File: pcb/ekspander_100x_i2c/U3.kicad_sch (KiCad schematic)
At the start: 6 parts, among them J10 DG127A-5.08-06P-14-00AH, J11 DG127A-5.08-06P-14-00AH, J8 DG127A-5.08-06P-14-00AH, J9 DG127A-5.08-06P-14-00AH, U3 MCP23017_SP, U4 MCP23017_SP

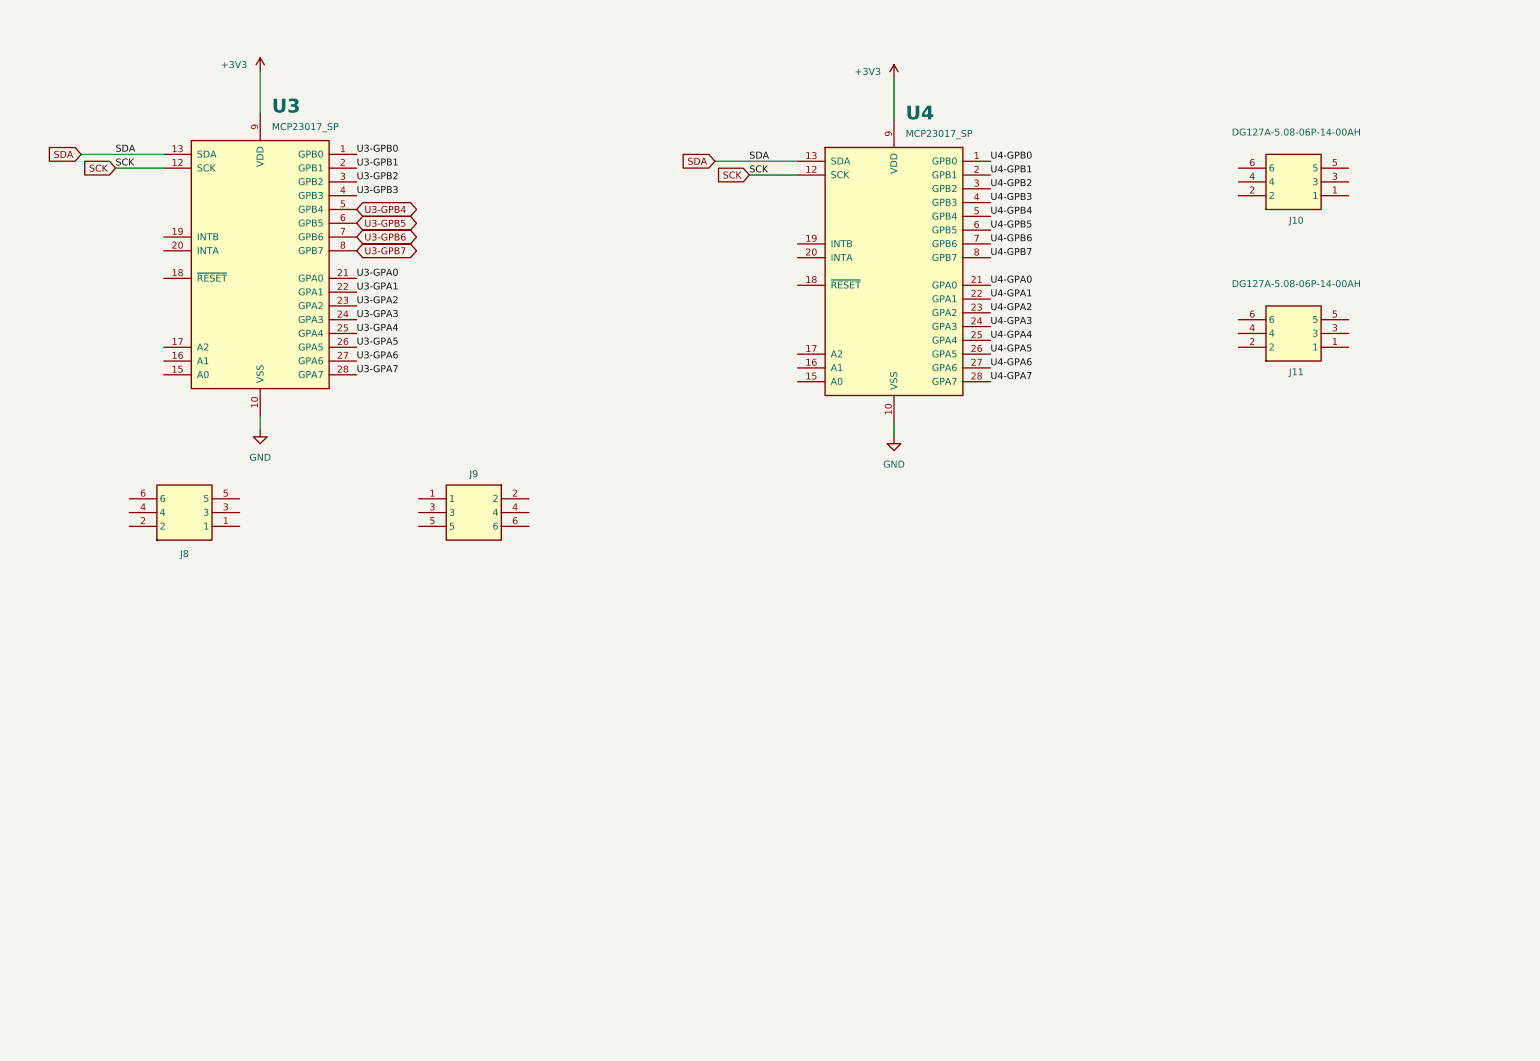
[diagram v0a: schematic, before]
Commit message: Ekspander U2 - U3 - U4 update
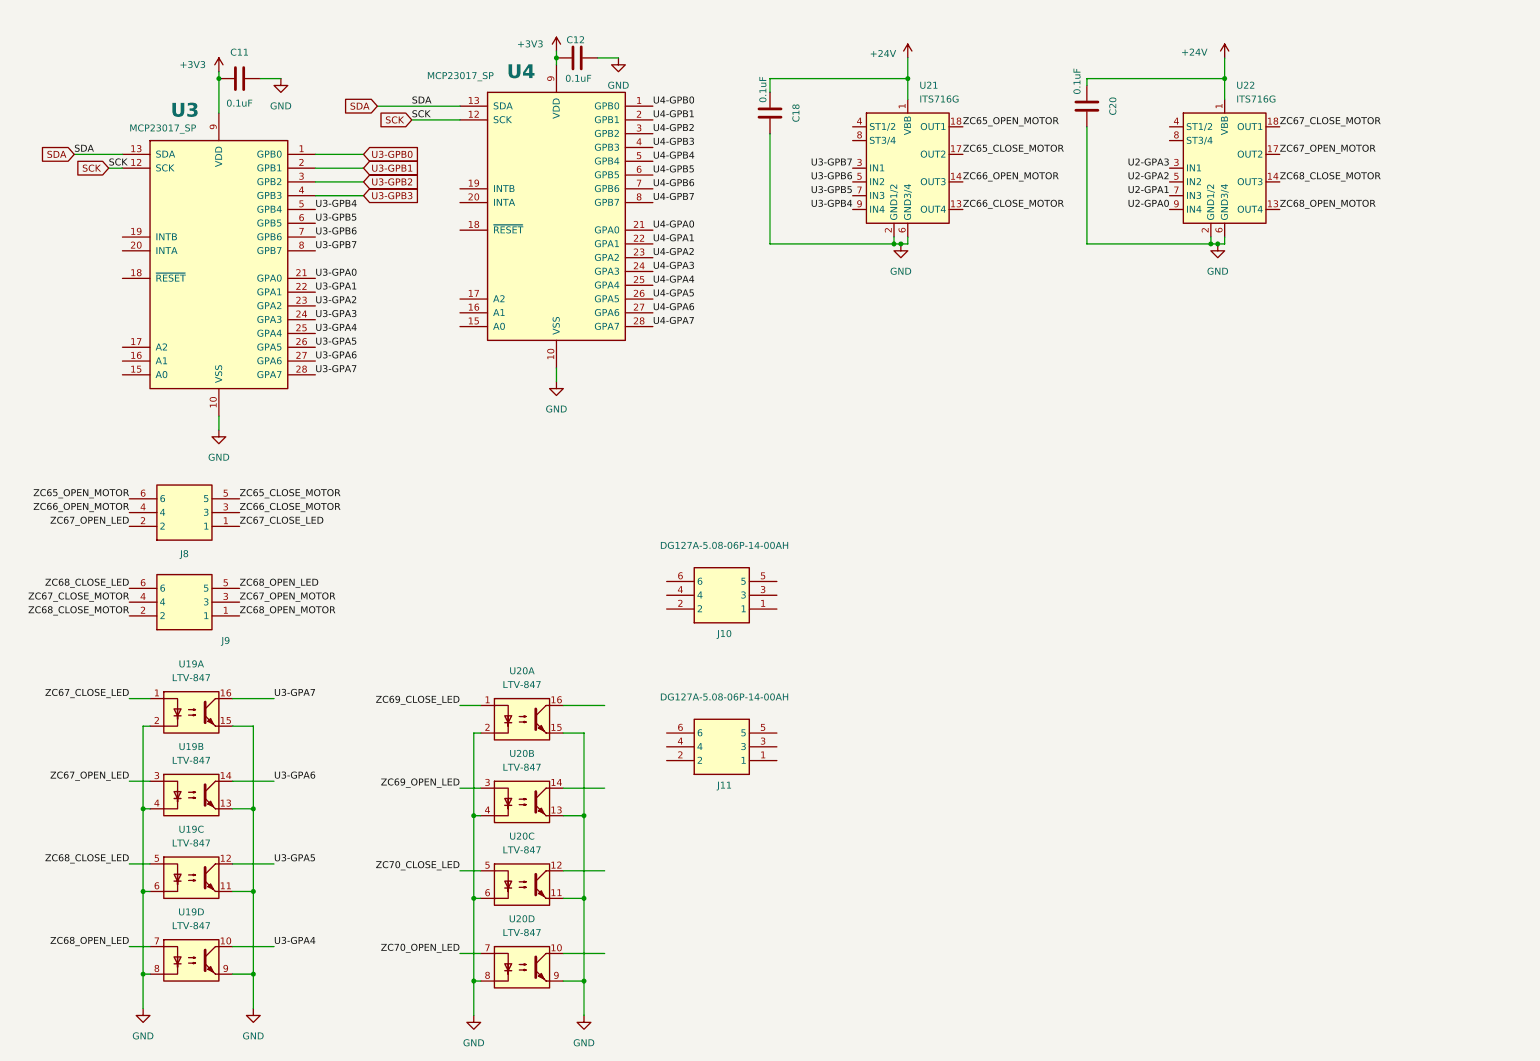
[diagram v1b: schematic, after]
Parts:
- added C11, C12, C18, C20: 0.1uF, Capacitor_SMD:C_0805_2012Metric_Pad1.18x1.45mm_HandSolder, symbol Device:C
- added U19, U20: LTV-847, Package_DIP:DIP-16_W7.62mm, symbol Isolator:LTV-847
- added U21, U22: ITS716G, Package_SO:SOIC-20W_7.5x12.8mm_P1.27mm, symbol Driver_FET:ITS716G
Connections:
- net +3V3: now also C11.1, C12.1
- net GND: now also C11.2, C12.2, C18.2, C20.2, U19.11, U19.13, U19.15, U19.2, U19.4, U19.6, U19.8, U19.9, U20.11, U20.13, U20.15, U20.2, U20.4, U20.6, U20.8, U20.9, U21.2 (GND1/2), U21.6 (GND3/4), U22.2 (GND1/2), U22.6 (GND3/4)
- net U3-GPA4: now also U19.10
- net U3-GPA5: now also U19.12
- net U3-GPA6: now also U19.14
- net U3-GPA7: now also U19.16
- net U3-GPB4: now also U21.9 (IN4)
- net U3-GPB5: now also U21.7 (IN3)
- net U3-GPB6: now also U21.5 (IN2)
- net U3-GPB7: now also U21.3 (IN1)
- net ZC67_CLOSE_LED: now reaches J8.1
- net ZC67_CLOSE_LED: now also U19.1
- net ZC67_OPEN_LED: now reaches J8.2
- net ZC67_OPEN_LED: now also U19.3
- net ZC66_CLOSE_MOTOR: now reaches J8.3
- net ZC66_CLOSE_MOTOR: now also U21.13 (OUT4)
- net ZC66_OPEN_MOTOR: now reaches J8.4
- net ZC66_OPEN_MOTOR: now also U21.14 (OUT3)
- net ZC65_CLOSE_MOTOR: now reaches J8.5
- net ZC65_CLOSE_MOTOR: now also U21.17 (OUT2)
- net ZC65_OPEN_MOTOR: now reaches J8.6
- net ZC65_OPEN_MOTOR: now also U21.18 (OUT1)
- net ZC68_OPEN_MOTOR: now reaches J9.1
- net ZC68_OPEN_MOTOR: now also U22.13 (OUT4)
- net ZC68_CLOSE_MOTOR: now reaches J9.2
- net ZC68_CLOSE_MOTOR: now also U22.14 (OUT3)
- net ZC67_OPEN_MOTOR: now reaches J9.3
- net ZC67_OPEN_MOTOR: now also U22.17 (OUT2)
- net ZC67_CLOSE_MOTOR: now reaches J9.4
- net ZC67_CLOSE_MOTOR: now also U22.18 (OUT1)
- net ZC68_OPEN_LED: now reaches J9.5
- net ZC68_OPEN_LED: now also U19.7
- net ZC68_CLOSE_LED: now reaches J9.6
- net ZC68_CLOSE_LED: now also U19.5
- new net +24V: C18.1, C20.1, U21.1 (VBB), U21.10 (VBB), U21.11 (VBB), U21.12 (VBB), U21.15 (VBB), U21.16 (VBB), U21.19 (VBB), U21.20 (VBB), U22.1 (VBB), U22.10 (VBB), U22.11 (VBB), U22.12 (VBB), U22.15 (VBB), U22.16 (VBB), U22.19 (VBB), U22.20 (VBB)
- new net U2-GPA0: U22.9 (IN4)
- new net U2-GPA1: U22.7 (IN3)
- new net U2-GPA2: U22.5 (IN2)
- new net U2-GPA3: U22.3 (IN1)
- new net ZC69_CLOSE_LED: U20.1
- new net ZC69_OPEN_LED: U20.3
- new net ZC70_CLOSE_LED: U20.5
- new net ZC70_OPEN_LED: U20.7
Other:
- moved on the sheet: J10, J11, J9, U3, U4

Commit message: Ekspander U5 - U6 update
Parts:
- added C21, C22: 0.1uF, Capacitor_SMD:C_0805_2012Metric_Pad1.18x1.45mm_HandSolder, symbol Device:C
- added U23, U24: ITS716G, Package_SO:SOIC-20W_7.5x12.8mm_P1.27mm, symbol Driver_FET:ITS716G
- added U25: LTV-847, Package_DIP:DIP-16_W7.62mm, symbol Isolator:LTV-847
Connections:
- net U2-GPA0 is gone; now on net U3-GPA7: U22.9 (IN4)
- net U2-GPA1 is gone; now on net U3-GPA6: U22.7 (IN3)
- net U2-GPA2 is gone; now on net U3-GPA5: U22.5 (IN2)
- net U2-GPA3 is gone; now on net U3-GPA4: U22.3 (IN1)
- net +24V: now also C21.1, C22.1, U23.1 (VBB), U23.10 (VBB), U23.11 (VBB), U23.12 (VBB), U23.15 (VBB), U23.16 (VBB), U23.19 (VBB), U23.20 (VBB), U24.1 (VBB), U24.10 (VBB), U24.11 (VBB), U24.12 (VBB), U24.15 (VBB), U24.16 (VBB), U24.19 (VBB), U24.20 (VBB)
- net GND: now also C21.2, C22.2, U23.2 (GND1/2), U23.6 (GND3/4), U24.2 (GND1/2), U24.6 (GND3/4), U25.11, U25.13, U25.15, U25.2, U25.4, U25.6, U25.8, U25.9
- net U3-GPA0: now also U19.10
- net U3-GPA1: now also U19.12
- net U3-GPA2: now also U19.14
- net U3-GPA3: now also U19.16
- net U3-GPA4: no longer U19.10
- net U3-GPA5: no longer U19.12
- net U3-GPA6: no longer U19.14
- net U3-GPA7: no longer U19.16
- net U4-GPA0: now also U25.16
- net U4-GPA1: now also U25.14
- net U4-GPA2: now also U25.12
- net U4-GPA3: now also U25.10
- net U4-GPA4: now also U24.9 (IN4)
- net U4-GPA5: now also U24.7 (IN3)
- net U4-GPA6: now also U24.5 (IN2)
- net U4-GPA7: now also U24.3 (IN1)
- net U4-GPB0: now also U20.16
- net U4-GPB1: now also U20.14
- net U4-GPB2: now also U20.12
- net U4-GPB3: now also U20.10
- net U4-GPB4: now also U23.9 (IN4)
- net U4-GPB5: now also U23.7 (IN3)
- net U4-GPB6: now also U23.5 (IN2)
- net U4-GPB7: now also U23.3 (IN1)
- net ZC69_CLOSE_LED: now also J10.3
- net ZC69_OPEN_LED: now also J10.4
- net ZC70_CLOSE_LED: now also J10.5
- net ZC70_OPEN_LED: now also J10.6
- net ZC72_OPEN_LED: now reaches J11.1
- net ZC72_OPEN_LED: now also U25.7
- net ZC72_CLOSE_LED: now reaches J11.2
- net ZC72_CLOSE_LED: now also U25.5
- net ZC71_OPEN_LED: now reaches J11.3
- net ZC71_OPEN_LED: now also U25.3
- net ZC71_CLOSE_LED: now reaches J11.4
- net ZC71_CLOSE_LED: now also U25.1
- net ZC70_CLOSE_MOTOR: now reaches J11.5
- net ZC70_CLOSE_MOTOR: now also U23.13 (OUT4)
- net ZC70_OPEN_MOTOR: now reaches J11.6
- net ZC70_OPEN_MOTOR: now also U23.14 (OUT3)
- net ZC69_CLOSE_MOTOR: now reaches J10.1
- net ZC69_CLOSE_MOTOR: now also U23.17 (OUT2)
- net ZC69_OPEN_MOTOR: now reaches J10.2
- net ZC69_OPEN_MOTOR: now also U23.18 (OUT1)
- new net ZC71_CLOSE_MOTOR: U24.17 (OUT2)
- new net ZC71_OPEN_MOTOR: U24.18 (OUT1)
- new net ZC72_CLOSE_MOTOR: U24.13 (OUT4)
- new net ZC72_OPEN_MOTOR: U24.14 (OUT3)
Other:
- moved on the sheet: J10, J11, J8, J9

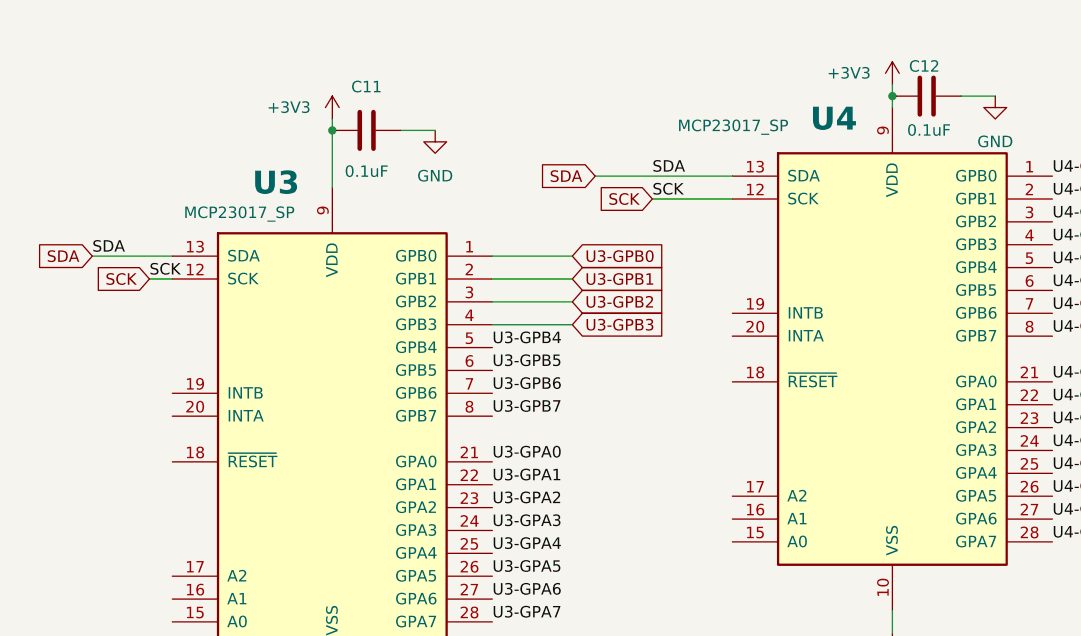
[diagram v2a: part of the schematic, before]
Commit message: Ekspander 24V update
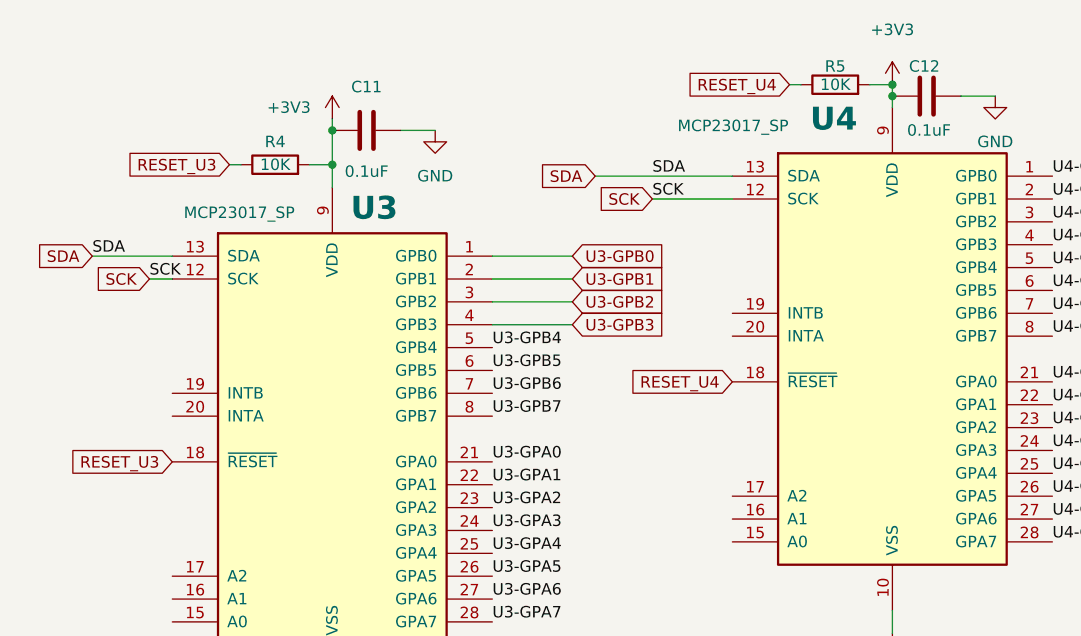
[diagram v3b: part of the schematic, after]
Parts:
- added R4, R5: 10K, PCM_Resistor_SMD_AKL:R_0805_2012Metric_Pad1.20x1.40mm_HandSolder, symbol Device:R
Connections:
- net +3V3: now also R4.2, R5.2
- net RESET_U3: now reaches U3.18 (~{RESET})
- net RESET_U3: now also R4.1
- net RESET_U4: now reaches U4.18 (~{RESET})
- net RESET_U4: now also R5.1
